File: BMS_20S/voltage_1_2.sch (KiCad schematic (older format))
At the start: 30 parts, among them U1901 TS1851ILT, U1902 TS1851ILT, U1903 TLP290-4

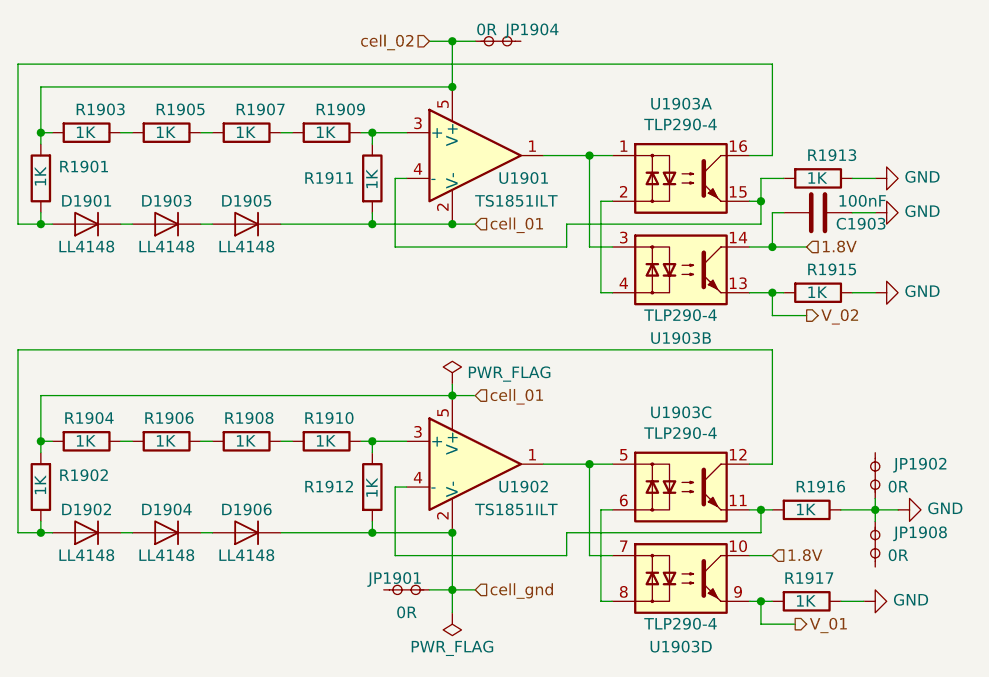
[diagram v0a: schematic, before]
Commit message: add current sense block to the schematic
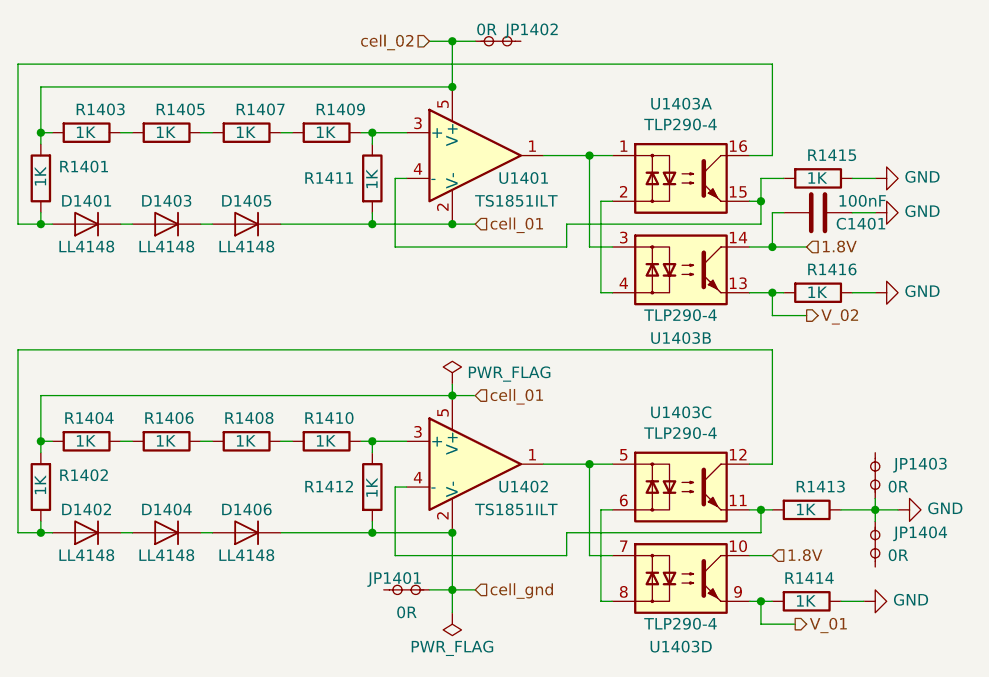
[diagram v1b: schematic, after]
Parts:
- renumbered C1903 to C501, D1901 to D501, D1902 to D502, D1903 to D503, D1904 to D504, D1905 to D505, D1906 to D506, JP1901 to JP501, JP1904 to JP502, JP1902 to JP503, JP1908 to JP504, R1901 to R501, R1902 to R502, R1903 to R503, R1904 to R504, R1905 to R505, R1906 to R506, R1907 to R507, R1908 to R508, R1909 to R509, R1910 to R510, R1911 to R511, R1912 to R512, R1916 to R513, R1917 to R514, R1913 to R515, R1915 to R516, U1901 to U501, U1902 to U502, U1903 to U503
